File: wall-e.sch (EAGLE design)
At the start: 70 parts, among them IC1 VREG-TS1117CW-3V3, T1 BC847, U1 TSM2306CX, U2 TSM2306CX, U3 TSM2306CX, U4 TSM2306CX, U5 TSM2306CX, U6 TSM2306CX, U7 TSM2306CX, U8 LM293AD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

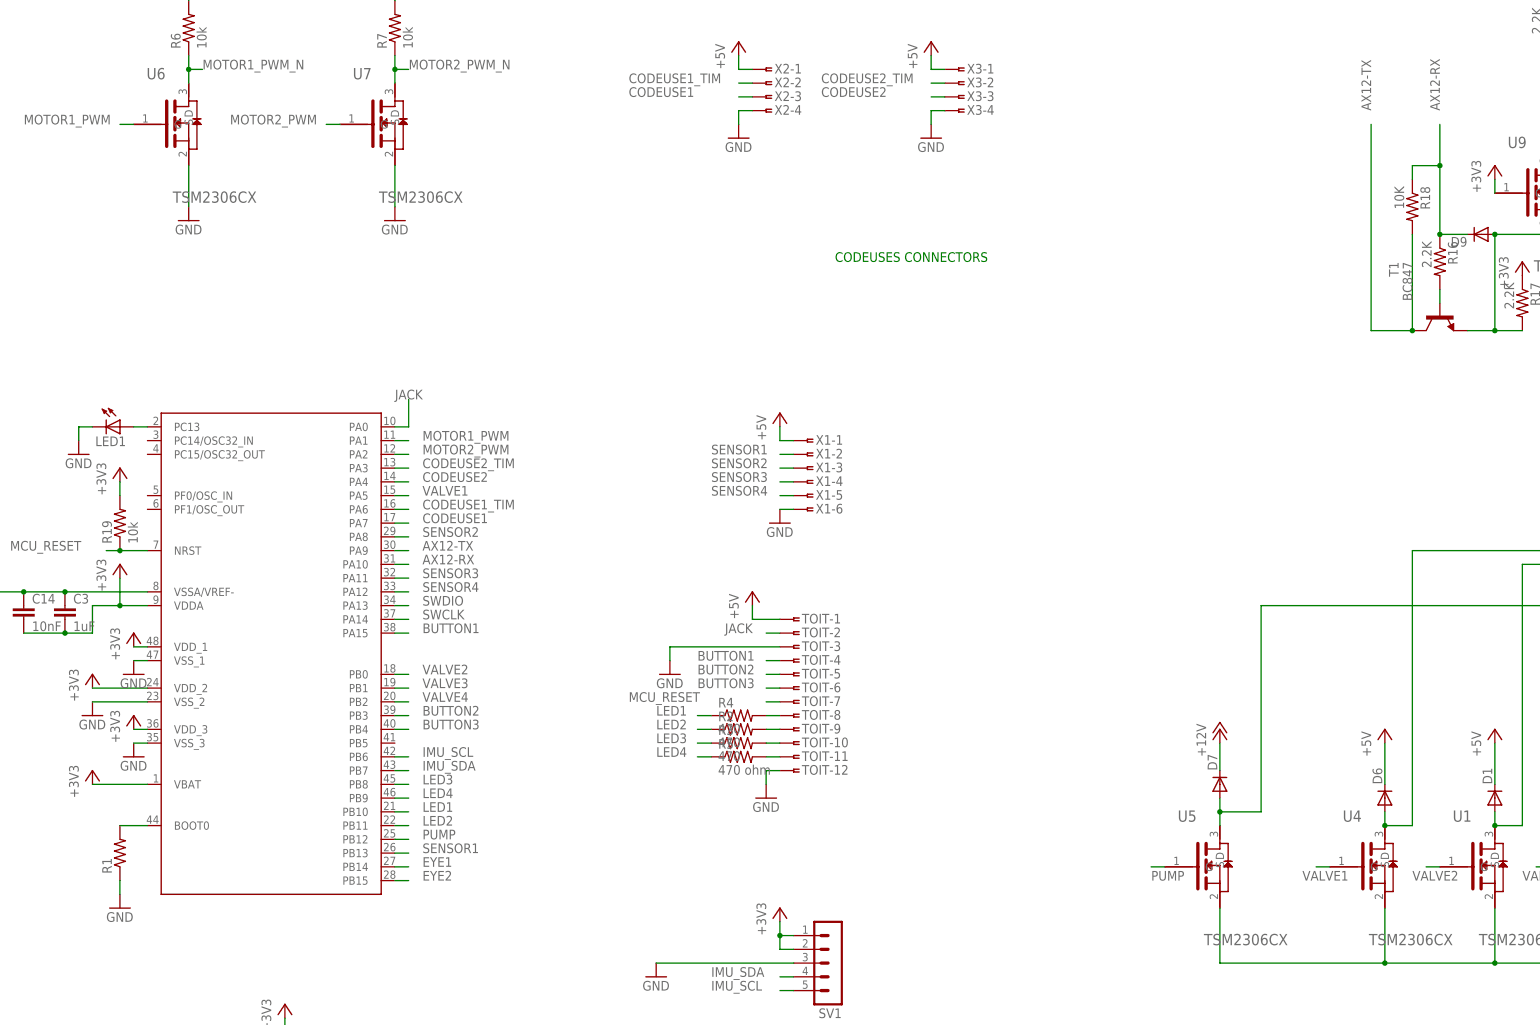
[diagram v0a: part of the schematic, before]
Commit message: Correction of some errors (capa size and RX/TX pinout)
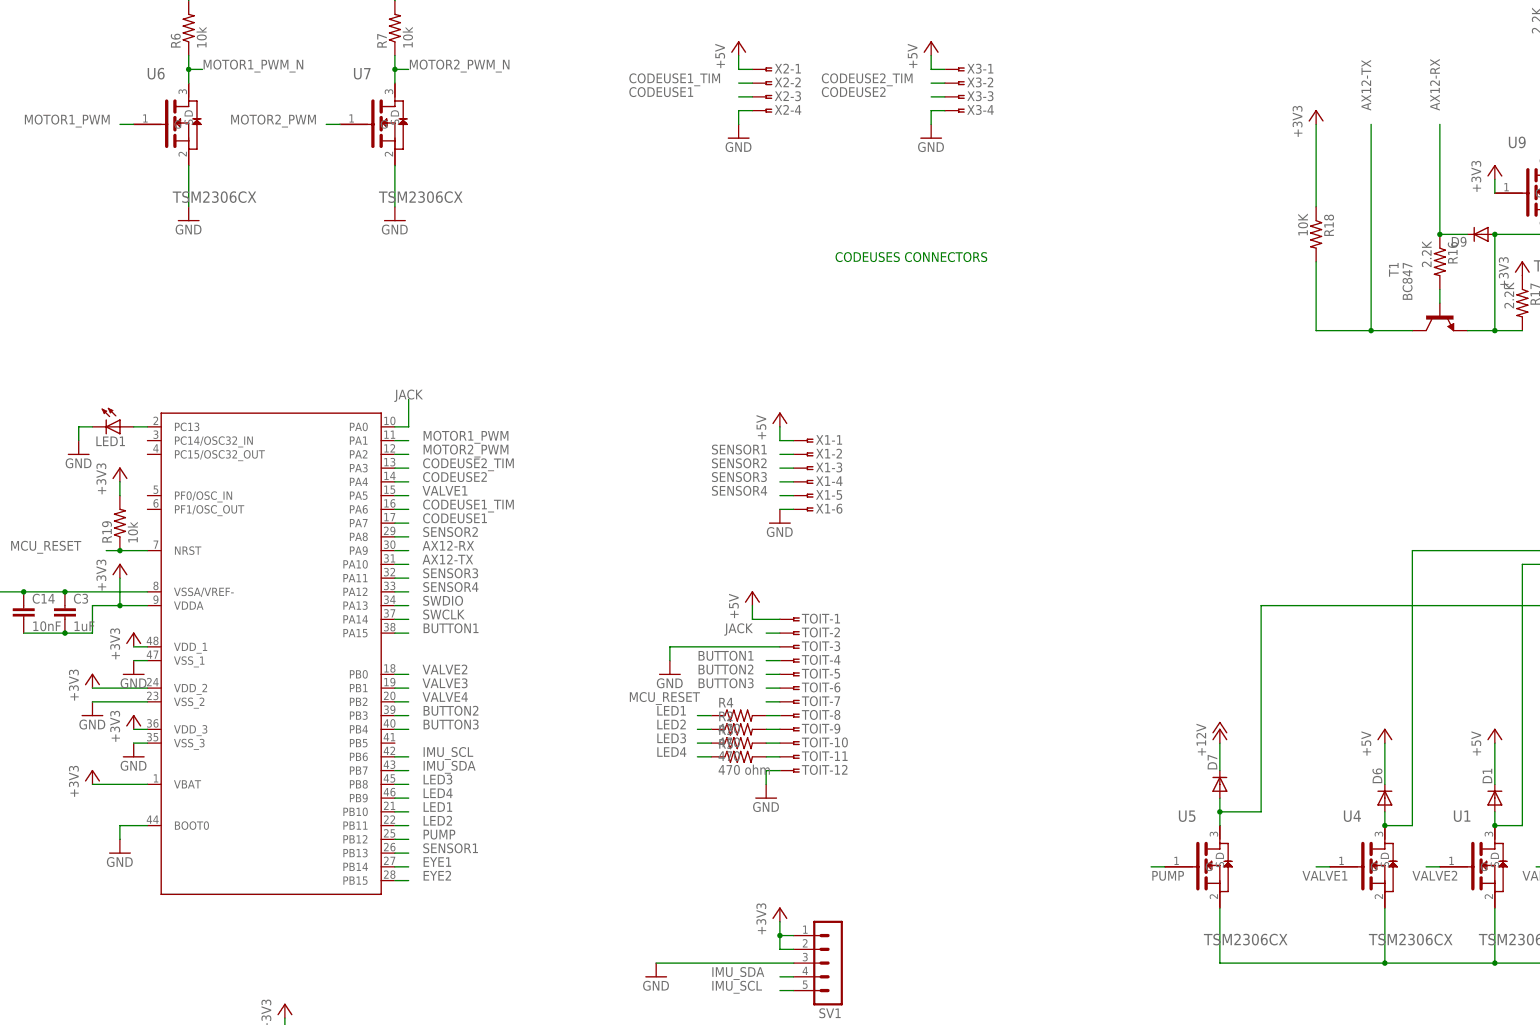
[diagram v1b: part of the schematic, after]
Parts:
- removed R1: (no value), rcl:R-US_R0805
- C1, C2: device rcl:C-EUC1206 -> rcl:C-EUC0805
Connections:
- removed net N$11: R1.2, U$1.BOOT0
- net +3V3: now also R18.1
- net AX12-RX: now also U$1.PA9; no longer R18.1, U$1.PA10
- net AX12-TX: now also U$1.PA10; no longer U$1.PA9
- net GND: now also U$1.BOOT0; no longer R1.1
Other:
- moved on the sheet: R18
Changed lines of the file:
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@@
 <?xml version="1.0" encoding="utf-8"?>
 <!DOCTYPE eagle SYSTEM "eagle.dtd">
-<eagle version="7.7.0">
+<eagle version="8.0.2">
 <drawing>
 <settings>
@@
 <part name="SV1" library="con-lstb" deviceset="MA05-1" device=""/>
 <part name="IC1" library="we-power" deviceset="VREG" device="-TS1117CW-3V3"/>
-<part name="C1" library="rcl" deviceset="C-EU" device="C1206" value="10uF"/>
-<part name="C2" library="rcl" deviceset="C-EU" device="C1206" value="10uF"/>
 <part name="GND1" library="supply1" deviceset="GND" device=""/>
 <part name="GND2" library="supply1" deviceset="GND" device=""/>
@@
 <part name="P+3" library="supply1" deviceset="+5V" device=""/>
 <part name="P+7" library="supply1" deviceset="+12V" device=""/>
-<part name="R1" library="rcl" deviceset="R-US_" device="R0805"/>
 <part name="R2" library="rcl" deviceset="R-US_" device="R0805" value="470"/>
 <part name="R3" library="rcl" deviceset="R-US_" device="R0805" value="470"/>
@@
 <part name="LED1" library="led" deviceset="LED" device="CHIP-LED0805"/>
 <part name="GND28" library="supply1" deviceset="GND" device=""/>
+<part name="C3" library="rcl" deviceset="C-EU" device="C0805" value="1uF"/>
+<part name="+3V16" library="supply1" deviceset="+3V3" device=""/>
+<part name="C1" library="rcl" deviceset="C-EU" device="C0805" value="10uF"/>
+<part name="C2" library="rcl" deviceset="C-EU" device="C0805" value="10uF"/>
 <part name="C14" library="rcl" deviceset="C-EU" device="C0805" value="10nF"/>
-<part name="C3" library="rcl" deviceset="C-EU" device="C0805" value="1uF"/>
 </parts>
 <sheets>
@@
 <instance part="SV1" gate="G$1" x="165.1" y="-7.62" rot="R180"/>
 <instance part="IC1" gate="IC" x="-50.8" y="96.52"/>
-<instance part="C1" gate="G$1" x="-66.04" y="88.9"/>
-<instance part="C2" gate="G$1" x="-38.1" y="88.9"/>
 <instance part="GND1" gate="1" x="-66.04" y="78.74"/>
 <instance part="GND2" gate="1" x="-50.8" y="78.74"/>
@@
 <instance part="P+3" gate="1" x="266.7" y="35.56"/>
 <instance part="P+7" gate="1" x="337.82" y="55.88"/>
-<instance part="R1" gate="G$1" x="33.02" y="12.7" rot="R90"/>
 <instance part="R2" gate="G$1" x="147.32" y="35.56"/>
 <instance part="R3" gate="G$1" x="147.32" y="33.02"/>
 <instance part="R4" gate="G$1" x="147.32" y="38.1"/>
 <instance part="R5" gate="G$1" x="147.32" y="30.48"/>
-<instance part="GND9" gate="1" x="33.02" y="2.54"/>
+<instance part="GND9" gate="1" x="33.02" y="12.7"/>
 <instance part="GND15" gate="1" x="307.34" y="-10.16"/>
 <instance part="GND16" gate="1" x="152.4" y="22.86"/>
@@
 <instance part="GND22" gate="1" x="-129.54" y="7.62"/>
 <instance part="R16" gate="G$1" x="276.86" y="121.92" rot="R270"/>
-<instance part="R18" gate="G$1" x="271.78" y="132.08" rot="R270"/>
+<instance part="R18" gate="G$1" x="254" y="127" rot="R270"/>
 <instance part="GND23" gate="1" x="312.42" y="134.62"/>
 <instance part="AX12" gate="G$1" x="314.96" y="144.78"/>
@@
 <instance part="LED1" gate="G$1" x="33.02" y="91.44" rot="R270"/>
 <instance part="GND28" gate="1" x="25.4" y="86.36"/>
+<instance part="C3" gate="G$1" x="22.86" y="58.42"/>
+<instance part="+3V16" gate="G$1" x="254" y="149.86"/>
+<instance part="C1" gate="G$1" x="-66.04" y="88.9"/>
+<instance part="C2" gate="G$1" x="-38.1" y="88.9"/>
 <instance part="C14" gate="G$1" x="15.24" y="58.42"/>
-<instance part="C3" gate="G$1" x="22.86" y="58.42"/>
 </instances>
 <busses>
@@
 <net name="GND" class="0">
 <segment>
-<pinref part="C1" gate="G$1" pin="2"/>
 <pinref part="GND1" gate="1" pin="GND"/>
 <wire x1="-66.04" y1="83.82" x2="-66.04" y2="81.28" width="0.1524" layer="91"/>
+<pinref part="C1" gate="G$1" pin="2"/>
 </segment>
 <segment>
@@
 </segment>
 <segment>
-<pinref part="C2" gate="G$1" pin="2"/>
 <pinref part="GND3" gate="1" pin="GND"/>
 <wire x1="-38.1" y1="83.82" x2="-38.1" y2="81.28" width="0.1524" layer="91"/>
+<pinref part="C2" gate="G$1" pin="2"/>
 </segment>
 <segment>
@@
 <pinref part="GND5" gate="1" pin="GND"/>
 <wire x1="38.1" y1="60.96" x2="22.86" y2="60.96" width="0.1524" layer="91"/>
+<wire x1="22.86" y1="60.96" x2="15.24" y2="60.96" width="0.1524" layer="91"/>
+<pinref part="C3" gate="G$1" pin="1"/>
+<junction x="22.86" y="60.96"/>
 <pinref part="C14" gate="G$1" pin="1"/>
-<wire x1="22.86" y1="60.96" x2="15.24" y2="60.96" width="0.1524" layer="91"/>
 <wire x1="15.24" y1="60.96" x2="7.62" y2="60.96" width="0.1524" layer="91"/>
 <junction x="15.24" y="60.96"/>
-<pinref part="C3" gate="G$1" pin="1"/>
-<junction x="22.86" y="60.96"/>
 </segment>
 <segment>
@@
 </segment>
 <segment>
-<pinref part="R1" gate="G$1" pin="1"/>
 <pinref part="GND9" gate="1" pin="GND"/>
-<wire x1="33.02" y1="7.62" x2="33.02" y2="5.08" width="0.1524" layer="91"/>
+<pinref part="U$1" gate="G$1" pin="BOOT0"/>
+<wire x1="38.1" y1="17.78" x2="33.02" y2="17.78" width="0.1524" layer="91"/>
+<wire x1="33.02" y1="17.78" x2="33.02" y2="15.24" width="0.1524" layer="91"/>
 </segment>
 <segment>
@@
 <net name="+5V" class="0">
 <segment>
-<pinref part="C1" gate="G$1" pin="1"/>
 <wire x1="-66.04" y1="91.44" x2="-66.04" y2="96.52" width="0.1524" layer="91"/>
 <pinref part="IC1" gate="IC" pin="VIN"/>
@@
 <junction x="-86.36" y="96.52"/>
 <wire x1="-86.36" y1="96.52" x2="-66.04" y2="96.52" width="0.1524" layer="91"/>
+<pinref part="C1" gate="G$1" pin="1"/>
 </segment>
 <segment>
@@
 <segment>
 <pinref part="IC1" gate="IC" pin="VOUT"/>
-<pinref part="C2" gate="G$1" pin="1"/>
 <wire x1="-40.64" y1="96.52" x2="-38.1" y2="96.52" width="0.1524" layer="91"/>
 <wire x1="-38.1" y1="96.52" x2="-38.1" y2="91.44" width="0.1524" layer="91"/>
@@
 <wire x1="-25.4" y1="96.52" x2="-38.1" y2="96.52" width="0.1524" layer="91"/>
 <junction x="-38.1" y="96.52"/>
+<pinref part="C2" gate="G$1" pin="1"/>
 </segment>
 <segment>
@@
 </segment>
 <segment>
-<pinref part="C14" gate="G$1" pin="2"/>
 <pinref part="C3" gate="G$1" pin="2"/>
 <wire x1="15.24" y1="53.34" x2="22.86" y2="53.34" width="0.1524" layer="91"/>
@@
 <wire x1="33.02" y1="63.5" x2="33.02" y2="58.42" width="0.1524" layer="91"/>
 <junction x="33.02" y="58.42"/>
+<pinref part="C14" gate="G$1" pin="2"/>
+</segment>
+<segment>
+<pinref part="R18" gate="G$1" pin="1"/>
+<wire x1="254" y1="132.08" x2="254" y2="147.32" width="0.1524" layer="91"/>
+<pinref part="+3V16" gate="G$1" pin="+3V3"/>
 </segment>
 </net>
@@
 </segment>
 </net>
-<net name="N$11" class="0">
-<segment>
-<pinref part="U$1" gate="G$1" pin="BOOT0"/>
-<pinref part="R1" gate="G$1" pin="2"/>
-<wire x1="38.1" y1="17.78" x2="33.02" y2="17.78" width="0.1524" layer="91"/>
-</segment>
-</net>
 <net name="BUTTON1" class="0">
 <segment>
@@
 <net name="AX12-RX" class="0">
 <segment>
-<pinref part="U$1" gate="G$1" pin="PA10"/>
-<wire x1="83.82" y1="66.04" x2="86.36" y2="66.04" width="0.1524" layer="91"/>
-<label x="88.9" y="66.04" size="1.778" layer="95"/>
-</segment>
-<segment>
-<wire x1="276.86" y1="147.32" x2="276.86" y2="139.7" width="0.1524" layer="91"/>
-<wire x1="276.86" y1="139.7" x2="271.78" y2="139.7" width="0.1524" layer="91"/>
 <label x="276.86" y="149.86" size="1.778" layer="95" rot="R90"/>
 <pinref part="R16" gate="G$1" pin="1"/>
@@
 <wire x1="276.86" y1="127" x2="281.94" y2="127" width="0.1524" layer="91"/>
 <junction x="276.86" y="127"/>
-<wire x1="276.86" y1="139.7" x2="276.86" y2="127" width="0.1524" layer="91"/>
-<junction x="276.86" y="139.7"/>
-<pinref part="R18" gate="G$1" pin="1"/>
-<wire x1="271.78" y1="137.16" x2="271.78" y2="139.7" width="0.1524" layer="91"/>
-</segment>
-</net>
-<net name="AX12-TX" class="0">
+<wire x1="276.86" y1="147.32" x2="276.86" y2="127" width="0.1524" layer="91"/>
+</segment>
 <segment>
 <pinref part="U$1" gate="G$1" pin="PA9"/>
@@
 <label x="88.9" y="68.58" size="1.778" layer="95"/>
 </segment>
-<segment>
-<pinref part="R18" gate="G$1" pin="2"/>
+</net>
+<net name="AX12-TX" class="0">
+<segment>
 <pinref part="T1" gate="G$1" pin="C"/>
-<wire x1="271.78" y1="109.22" x2="271.78" y2="127" width="0.1524" layer="91"/>
 <wire x1="271.78" y1="109.22" x2="264.16" y2="109.22" width="0.1524" layer="91"/>
-<junction x="271.78" y="109.22"/>
 <wire x1="264.16" y1="109.22" x2="264.16" y2="147.32" width="0.1524" layer="91"/>
 <label x="264.16" y="149.86" size="1.778" layer="95" rot="R90"/>
+<wire x1="264.16" y1="109.22" x2="254" y2="109.22" width="0.1524" layer="91"/>
+<junction x="264.16" y="109.22"/>
+<pinref part="R18" gate="G$1" pin="2"/>
+<wire x1="254" y1="109.22" x2="254" y2="121.92" width="0.1524" layer="91"/>
+</segment>
+<segment>
+<pinref part="U$1" gate="G$1" pin="PA10"/>
+<wire x1="83.82" y1="66.04" x2="86.36" y2="66.04" width="0.1524" layer="91"/>
+<label x="88.9" y="66.04" size="1.778" layer="95"/>
 </segment>
 </net>
@@
 </sheet>
 </sheets>
+<errors>
+</errors>
 </schematic>
 </drawing>

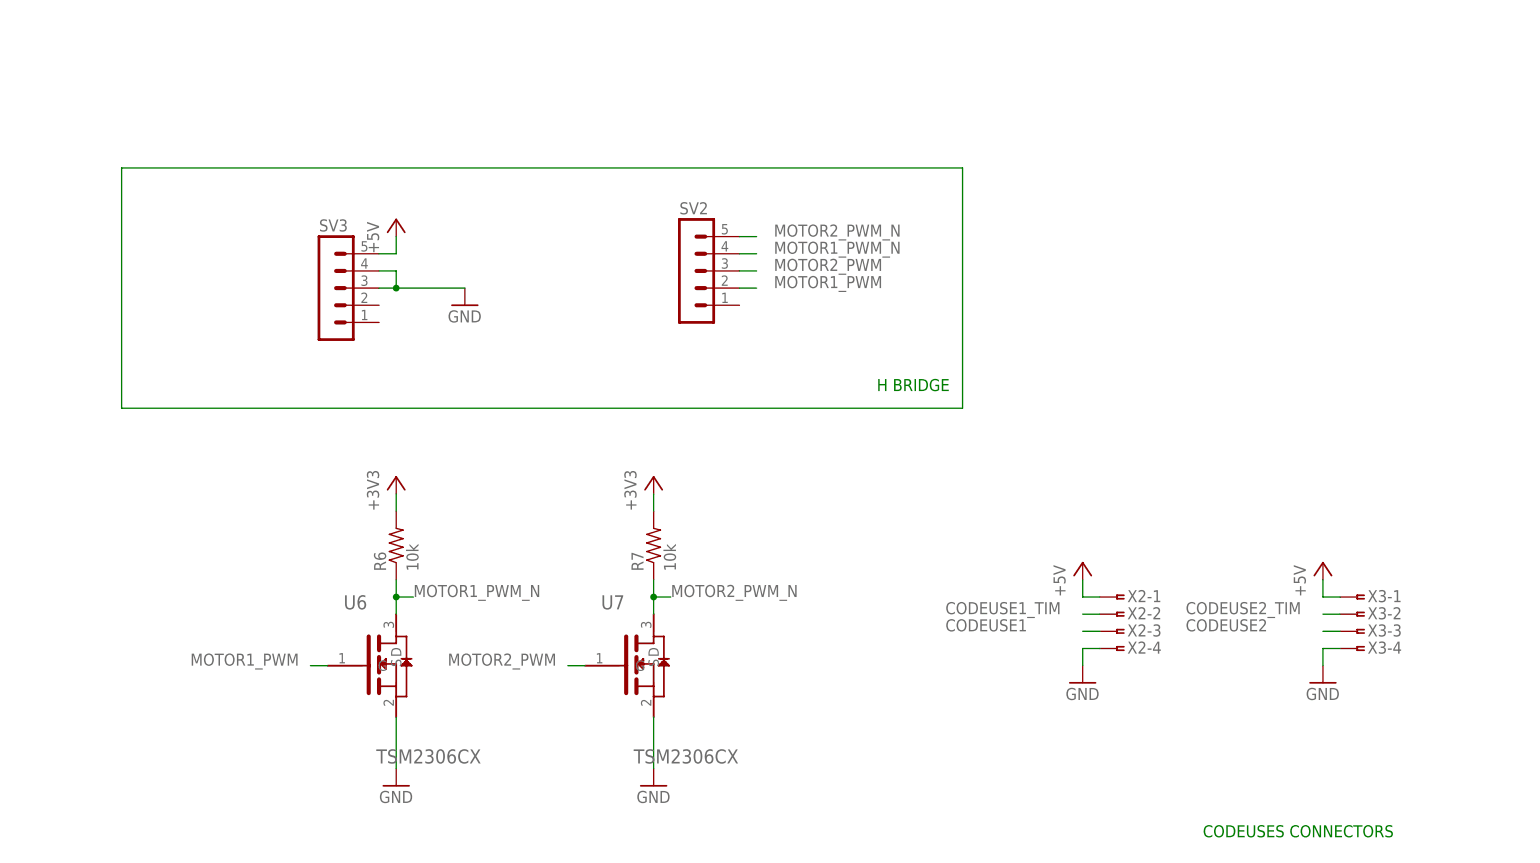
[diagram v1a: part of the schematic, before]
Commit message: Change in the H bridge
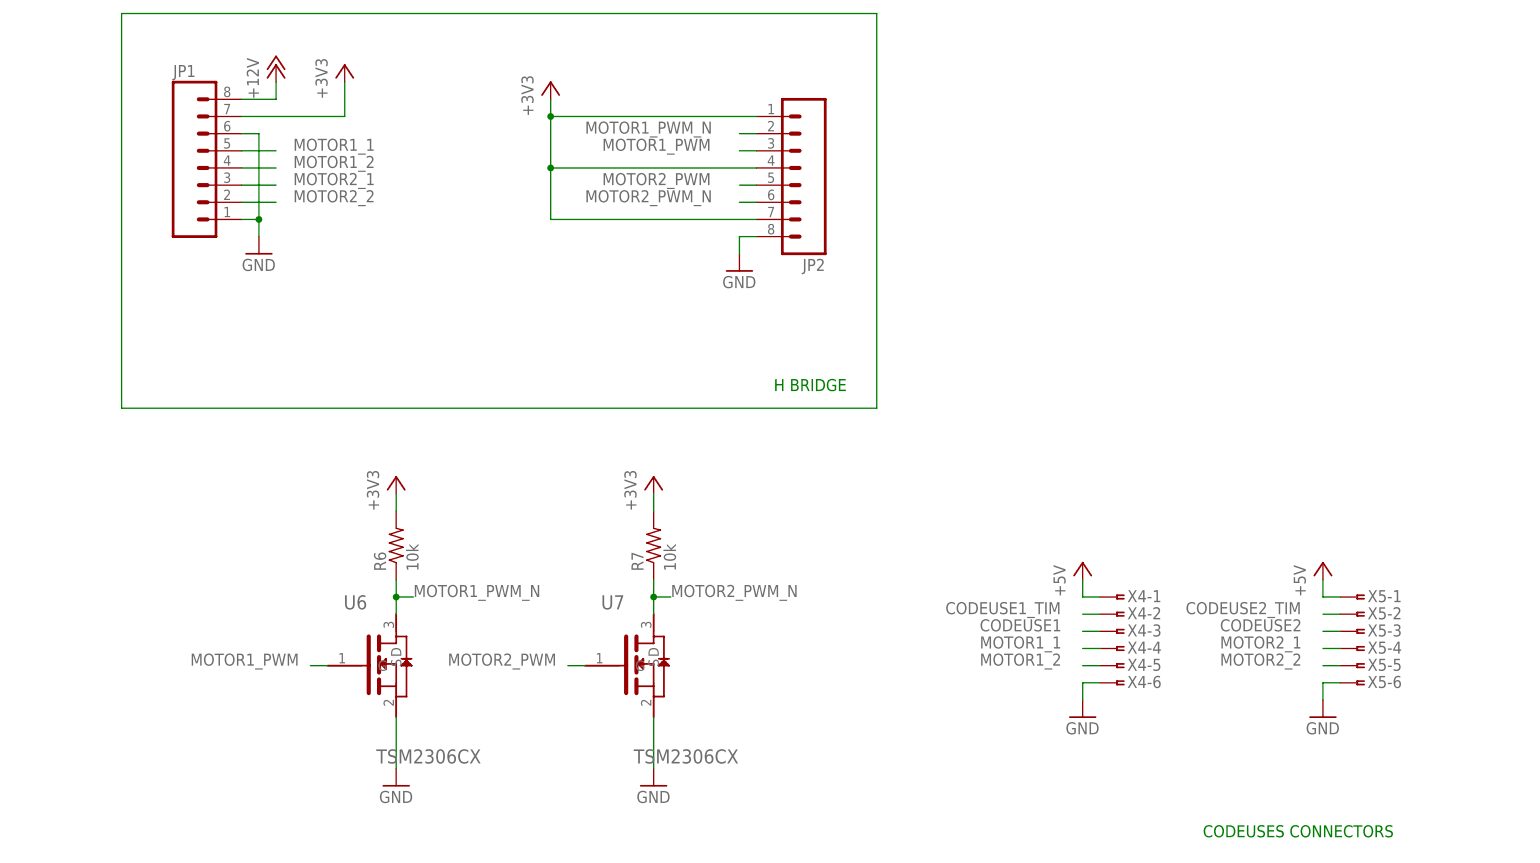
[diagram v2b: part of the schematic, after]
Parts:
- removed SV2, SV3: (no value), con-lstb:MA05-1
- removed X2, X3: (no value), con-amp:SMDTOP-4
- added JP1, JP2: (no value), SparkFun:M08LONGPADS
- added X4, X5: (no value), con-amp:SMDTOP-6
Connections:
- new net MOTOR1_1: JP1.5, X4-4.1
- new net MOTOR1_2: JP1.4, X4-5.1
- new net MOTOR2_1: JP1.3, X5-4.1
- new net MOTOR2_2: JP1.2, X5-5.1
- net +12V: now also JP1.8
- net +3V3: now also JP1.7, JP2.1, JP2.4, JP2.7
- net +5V: now also X4-1.1, X5-1.1; no longer SV3.5, X2-1.1, X3-1.1
- net CODEUSE1: now also X4-3.1; no longer X2-3.1
- net CODEUSE1_TIM: now also X4-2.1; no longer X2-2.1
- net CODEUSE2: now also X5-3.1; no longer X3-3.1
- net CODEUSE2_TIM: now also X5-2.1; no longer X3-2.1
- net GND: now also JP1.1, JP1.6, JP2.8, X4-6.1, X5-6.1; no longer SV3.3, SV3.4, X2-4.1, X3-4.1
- net MOTOR1_PWM: now also JP2.3; no longer SV2.2
- net MOTOR1_PWM_N: now also JP2.2; no longer SV2.4
- net MOTOR2_PWM: now also JP2.5; no longer SV2.3
- net MOTOR2_PWM_N: now also JP2.6; no longer SV2.5
